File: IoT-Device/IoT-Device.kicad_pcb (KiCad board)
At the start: 4 copper layers, 100 x 70 mm, 61 parts, among them J1 USB-C, J2 Conn_01x02, J3 SWD, SW1 RESET, SW2 BOOT_MODE, SW3 B1, SW4 B2, U1 BD33GA5WEFJ, U2 STM32U585VI, U3 BQ24074RGT, U4 ESP32-C3-WROOM-02

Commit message: change two ESP32 pins for slightly more appropriate ones on STM32 (ESP_BUSY->PB2 (SPI1_RDY)
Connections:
- U2 pad 35: /ESP_RESET -> unconnected-(U2-PB0-Pad35)
- U2 pad 36: /ESP_BUSY -> /ESP_RESET
- U2 pad 37: unconnected-(U2-PB2-Pad37) -> /ESP_BUSY
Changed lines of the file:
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@@
 	(net 102 "/SWO")
 	(net 103 "/SWDIO")
-	(net 104 "unconnected-(U2-PB2-Pad37)")
-	(net 105 "/SWCLK")
-	(net 106 "unconnected-(U2-PC9-Pad66)")
-	(net 107 "unconnected-(U2-PC15-Pad9)")
-	(net 108 "Net-(D4-K)")
-	(net 109 "unconnected-(U2-PA1-Pad24)")
-	(net 110 "unconnected-(U2-PE5-Pad4)")
-	(net 111 "unconnected-(U3-ITERM-Pad15)")
-	(net 112 "unconnected-(U3-TMR-Pad14)")
-	(net 113 "Net-(U4-IO2)")
-	(net 114 "unconnected-(U4-IO18-Pad13)")
-	(net 115 "unconnected-(U4-IO1-Pad17)")
-	(net 116 "unconnected-(U4-IO19-Pad14)")
-	(net 117 "unconnected-(U4-IO0-Pad18)")
-	(net 118 "unconnected-(U4-IO3-Pad15)")
+	(net 104 "/SWCLK")
+	(net 105 "unconnected-(U2-PC9-Pad66)")
+	(net 106 "unconnected-(U2-PC15-Pad9)")
+	(net 107 "Net-(D4-K)")
+	(net 108 "unconnected-(U2-PA1-Pad24)")
+	(net 109 "unconnected-(U2-PE5-Pad4)")
+	(net 110 "unconnected-(U3-ITERM-Pad15)")
+	(net 111 "unconnected-(U3-TMR-Pad14)")
+	(net 112 "Net-(U4-IO2)")
+	(net 113 "unconnected-(U4-IO18-Pad13)")
+	(net 114 "unconnected-(U4-IO1-Pad17)")
+	(net 115 "unconnected-(U4-IO19-Pad14)")
+	(net 116 "unconnected-(U4-IO0-Pad18)")
+	(net 117 "unconnected-(U4-IO3-Pad15)")
+	(net 118 "unconnected-(U2-PB0-Pad35)")
 	(footprint "Capacitor_SMD:C_0603_1608Metric"
 		(layer "F.Cu")
@@
 			(layers "F.Cu" "F.Mask" "F.Paste")
 			(roundrect_rratio 0.25)
-			(net 110 "unconnected-(U2-PE5-Pad4)")
+			(net 109 "unconnected-(U2-PE5-Pad4)")
 			(pinfunction "PE5")
 			(pintype "bidirectional+no_connect")
@@
 			(layers "F.Cu" "F.Mask" "F.Paste")
 			(roundrect_rratio 0.25)
-			(net 107 "unconnected-(U2-PC15-Pad9)")
+			(net 106 "unconnected-(U2-PC15-Pad9)")
 			(pinfunction "PC15")
 			(pintype "bidirectional+no_connect")
@@
 			(layers "F.Cu" "F.Mask" "F.Paste")
 			(roundrect_rratio 0.25)
-			(net 109 "unconnected-(U2-PA1-Pad24)")
+			(net 108 "unconnected-(U2-PA1-Pad24)")
 			(pinfunction "PA1")
 			(pintype "bidirectional+no_connect")
@@
 			(layers "F.Cu" "F.Mask" "F.Paste")
 			(roundrect_rratio 0.25)
-			(net 36 "/ESP_RESET")
+			(net 118 "unconnected-(U2-PB0-Pad35)")
 			(pinfunction "PB0")
-			(pintype "bidirectional")
+			(pintype "bidirectional+no_connect")
 		)
 		(pad "36" smd roundrect
@@
 			(layers "F.Cu" "F.Mask" "F.Paste")
 			(roundrect_rratio 0.25)
-			(net 51 "/ESP_BUSY")
+			(net 36 "/ESP_RESET")
 			(pinfunction "PB1")
 			(pintype "bidirectional")
@@
 			(layers "F.Cu" "F.Mask" "F.Paste")
 			(roundrect_rratio 0.25)
-			(net 104 "unconnected-(U2-PB2-Pad37)")
+			(net 51 "/ESP_BUSY")
 			(pinfunction "PB2")
-			(pintype "bidirectional+no_connect")
+			(pintype "bidirectional")
 		)
 		(pad "38" smd roundrect
@@
 			(layers "F.Cu" "F.Mask" "F.Paste")
 			(roundrect_rratio 0.25)
-			(net 106 "unconnected-(U2-PC9-Pad66)")
+			(net 105 "unconnected-(U2-PC9-Pad66)")
 			(pinfunction "PC9")
 			(pintype "bidirectional+no_connect")
@@
 			(layers "F.Cu" "F.Mask" "F.Paste")
 			(roundrect_rratio 0.25)
-			(net 105 "/SWCLK")
+			(net 104 "/SWCLK")
 			(pinfunction "PA14")
 			(pintype "bidirectional")
@@
 			(size 1.5 0.9)
 			(layers "F.Cu" "F.Mask" "F.Paste")
-			(net 114 "unconnected-(U4-IO18-Pad13)")
+			(net 113 "unconnected-(U4-IO18-Pad13)")
 			(pinfunction "IO18")
 			(pintype "bidirectional+no_connect")
@@
 			(size 1.5 0.9)
 			(layers "F.Cu" "F.Mask" "F.Paste")
-			(net 116 "unconnected-(U4-IO19-Pad14)")
+			(net 115 "unconnected-(U4-IO19-Pad14)")
 			(pinfunction "IO19")
 			(pintype "bidirectional+no_connect")
@@
 			(size 1.5 0.9)
 			(layers "F.Cu" "F.Mask" "F.Paste")
-			(net 118 "unconnected-(U4-IO3-Pad15)")
+			(net 117 "unconnected-(U4-IO3-Pad15)")
 			(pinfunction "IO3")
 			(pintype "bidirectional+no_connect")
@@
 			(size 1.5 0.9)
 			(layers "F.Cu" "F.Mask" "F.Paste")
-			(net 113 "Net-(U4-IO2)")
+			(net 112 "Net-(U4-IO2)")
 			(pinfunction "IO2")
 			(pintype "bidirectional")
@@
 			(size 1.5 0.9)
 			(layers "F.Cu" "F.Mask" "F.Paste")
-			(net 115 "unconnected-(U4-IO1-Pad17)")
+			(net 114 "unconnected-(U4-IO1-Pad17)")
 			(pinfunction "IO1")
 			(pintype "bidirectional+no_connect")
@@
 			(size 1.5 0.9)
 			(layers "F.Cu" "F.Mask" "F.Paste")
-			(net 117 "unconnected-(U4-IO0-Pad18)")
+			(net 116 "unconnected-(U4-IO0-Pad18)")
 			(pinfunction "IO0")
 			(pintype "bidirectional+no_connect")
@@
 			(layers "F.Cu" "F.Mask" "F.Paste")
 			(roundrect_rratio 0.25)
-			(net 108 "Net-(D4-K)")
+			(net 107 "Net-(D4-K)")
 			(pintype "passive")
 		)
@@
 			(size 2.4 0.74)
 			(layers "F.Cu" "F.Mask" "F.Paste")
-			(net 105 "/SWCLK")
+			(net 104 "/SWCLK")
 			(pinfunction "SWCLK/TCK")
 			(pintype "output")
@@
 			(layers "F.Cu" "F.Mask" "F.Paste")
 			(roundrect_rratio 0.25)
-			(net 108 "Net-(D4-K)")
+			(net 107 "Net-(D4-K)")
 			(pinfunction "K")
 			(pintype "passive")
@@
 			(layers "F.Cu" "F.Mask" "F.Paste")
 			(roundrect_rratio 0.25)
-			(net 113 "Net-(U4-IO2)")
+			(net 112 "Net-(U4-IO2)")
 			(pintype "passive")
 		)
@@
 			(layers "F.Cu" "F.Mask" "F.Paste")
 			(roundrect_rratio 0.25)
-			(net 112 "unconnected-(U3-TMR-Pad14)")
+			(net 111 "unconnected-(U3-TMR-Pad14)")
 			(pinfunction "TMR")
 			(pintype "input+no_connect")
@@
 			(layers "F.Cu" "F.Mask" "F.Paste")
 			(roundrect_rratio 0.25)
-			(net 111 "unconnected-(U3-ITERM-Pad15)")
+			(net 110 "unconnected-(U3-ITERM-Pad15)")
 			(pinfunction "ITERM")
 			(pintype "input+no_connect")
@@
 	)
 	(segment
-		(start 39.201 84.101)
-		(end 72.1674 84.101)
+		(start 72.1674 84.101)
+		(end 39.201 84.101)
 		(width 0.2)
 		(layer "F.Cu")
@@
 	)
 	(segment
-		(start 86.825 69.4434)
-		(end 86.825 66.175)
+		(start 87.325 66.175)
+		(end 87.325 68.9434)
 		(width 0.2)
 		(layer "F.Cu")
@@
 	)
 	(segment
-		(start 72.1674 84.101)
-		(end 86.825 69.4434)
+		(start 87.325 68.9434)
+		(end 72.1674 84.101)
 		(width 0.2)
 		(layer "F.Cu")
@@
 	)
 	(segment
-		(start 38.7729 82.74)
-		(end 72.09 82.74)
+		(start 87.825 66.175)
+		(end 87.825 69.29193)
 		(width 0.2)
 		(layer "F.Cu")
@@
 	)
 	(segment
-		(start 87.325 69.79193)
-		(end 87.325 66.175)
+		(start 38.7729 82.74)
+		(end 72.09 82.74)
 		(width 0.2)
 		(layer "F.Cu")
@@
 	)
 	(segment
-		(start 36.8 80.7671)
-		(end 38.7729 82.74)
+		(start 87.825 69.29193)
+		(end 86.818465 70.298465)
 		(width 0.2)
 		(layer "F.Cu")
@@
 	)
 	(segment
-		(start 86.818465 70.298465)
-		(end 87.325 69.79193)
+		(start 36.8 80.7671)
+		(end 38.7729 82.74)
 		(width 0.2)
 		(layer "F.Cu")
@@
 		(width 0.2)
 		(layer "F.Cu")
-		(net 105)
+		(net 104)
 	)
 	(segment
@@
 		(width 0.2)
 		(layer "F.Cu")
-		(net 105)
+		(net 104)
 	)
 	(segment
@@
 		(width 0.2)
 		(layer "F.Cu")
-		(net 105)
+		(net 104)
 	)
 	(segment
@@
 		(width 0.2)
 		(layer "F.Cu")
-		(net 105)
+		(net 104)
 	)
 	(segment
@@
 		(width 0.2)
 		(layer "F.Cu")
-		(net 105)
+		(net 104)
 	)
 	(segment
@@
 		(width 0.2)
 		(layer "F.Cu")
-		(net 105)
+		(net 104)
 	)
 	(segment
@@
 		(width 0.2)
 		(layer "F.Cu")
-		(net 105)
+		(net 104)
 	)
 	(via
@@
 		(drill 0.3)
 		(layers "F.Cu" "B.Cu")
-		(net 105)
+		(net 104)
 	)
 	(via
@@
 		(drill 0.3)
 		(layers "F.Cu" "B.Cu")
-		(net 105)
+		(net 104)
 	)
 	(segment
@@
 		(width 0.2)
 		(layer "B.Cu")
-		(net 105)
+		(net 104)
 	)
 	(segment
@@
 		(width 0.2)
 		(layer "B.Cu")
-		(net 105)
+		(net 104)
 	)
 	(segment
@@
 		(width 0.2)
 		(layer "B.Cu")
-		(net 105)
+		(net 104)
 	)
 	(segment
@@
 		(width 0.2)
 		(layer "F.Cu")
-		(net 108)
+		(net 107)
 	)
 	(segment
@@
 		(width 0.2)
 		(layer "F.Cu")
-		(net 113)
+		(net 112)
 	)
 	(zone

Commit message: update SW2 GND routing
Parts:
- added R22: 10k, Resistor_SMD:R_0603_1608Metric, F.Cu at (69.9, 26.1)
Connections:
- SW2 pad 1: GND -> Net-(SW2-A)
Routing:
- net Net-(SW2-A): track 0.00 -> 2.30 mm
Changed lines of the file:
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@@
 			(drillshape 0)
 			(scaleselection 1)
-			(outputdirectory "production_manual/drill/")
+			(outputdirectory "production_manual/")
 		)
 	)
@@
 	(net 117 "unconnected-(U4-IO3-Pad15)")
 	(net 118 "unconnected-(U2-PB0-Pad35)")
+	(net 119 "Net-(SW2-A)")
 	(footprint "Capacitor_SMD:C_0603_1608Metric"
 		(layer "F.Cu")
@@
 		(descr "Ultraminiature Surface Mount Slide Switch, right-angle, https://www.ckswitches.com/media/1424/pcm.pdf")
 		(property "Reference" "SW2"
-			(at -5.9 -1.325 0)
+			(at -6.01 1.285 0)
 			(layer "F.SilkS")
 			(effects
@@
 		)
 		(property "Value" "BOOT_MODE"
-			(at -7.2 -3.225 0)
+			(at -8.76 -0.235 0)
 			(layer "F.Fab")
 			(effects
@@
 			(layer "F.Fab")
 		)
+		(fp_text user "${REFERENCE}"
+			(at 0 -3.2 180)
+			(layer "F.Fab")
+			(effects
+				(font
+					(size 1 1)
+					(thickness 0.15)
+				)
+			)
+		)
 		(pad "" smd rect
 			(at -3.65 -0.78 180)
@@
 			(size 0.7 1.5)
 			(layers "F.Cu" "F.Mask" "F.Paste")
-			(net 99 "GND")
+			(net 119 "Net-(SW2-A)")
 			(pinfunction "A")
 			(pintype "passive")
@@
 		)
 	)
+	(footprint "Resistor_SMD:R_0603_1608Metric"
+		(layer "F.Cu")
+		(at 69.88 26.1)
+		(descr "Resistor SMD 0603 (1608 Metric), square (rectangular) end terminal, IPC-7351 nominal, (Body size source: IPC-SM-782 page 72, https://www.pcb-3d.com/wordpress/wp-content/uploads/ipc-sm-782a_amendment_1_and_2.pdf), generated with kicad-footprint-generator")
+		(tags "resistor")
+		(property "Reference" "R22"
+			(at -2.87 0.64 0)
+			(layer "F.SilkS")
+			(effects
+				(font
+					(size 1 1)
+					(thickness 0.15)
+				)
+			)
+		)
+		(property "Value" "10k"
+			(at 0 1.43 0)
+			(layer "F.Fab")
+			(effects
+				(font
+					(size 1 1)
+					(thickness 0.15)
+				)
+			)
+		)
+		(property "Datasheet" "~"
+			(at 0 0 0)
+			(layer "F.Fab")
+			(hide yes)
+			(effects
+				(font
+					(size 1.27 1.27)
+					(thickness 0.15)
+				)
+			)
+		)
+		(property "Description" "Resistor"
+			(at 0 0 0)
+			(layer "F.Fab")
+			(hide yes)
+			(effects
+				(font
+					(size 1.27 1.27)
+					(thickness 0.15)
+				)
+			)
+		)
+		(property ki_fp_filters "R_*")
+		(sheetname "/")
+		(sheetfile "IoT-Device.kicad_sch")
+		(attr smd)
+		(fp_line
+			(start -0.237258 -0.5225)
+			(end 0.237258 -0.5225)
+			(stroke
+				(width 0.12)
+				(type solid)
+			)
+			(layer "F.SilkS")
+		)
+		(fp_line
+			(start -0.237258 0.5225)
+			(end 0.237258 0.5225)
+			(stroke
+				(width 0.12)
+				(type solid)
+			)
+			(layer "F.SilkS")
+		)
+		(fp_rect
+			(start -1.48 -0.73)
+			(end 1.48 0.73)
+			(stroke
+				(width 0.05)
+				(type solid)
+			)
+			(fill no)
+			(layer "F.CrtYd")
+		)
+		(fp_rect
+			(start -0.8 -0.4125)
+			(end 0.8 0.4125)
+			(stroke
+				(width 0.1)
+				(type solid)
+			)
+			(fill no)
+			(layer "F.Fab")
+		)
+		(fp_text user "${REFERENCE}"
+			(at 0 0 0)
+			(layer "F.Fab")
+			(effects
+				(font
+					(size 0.4 0.4)
+					(thickness 0.06)
+				)
+			)
+		)
+		(pad "1" smd roundrect
+			(at -0.825 0)
+			(size 0.8 0.95)
+			(layers "F.Cu" "F.Mask" "F.Paste")
+			(roundrect_rratio 0.25)
+			(net 119 "Net-(SW2-A)")
+			(pintype "passive")
+		)
+		(pad "2" smd roundrect
+			(at 0.825 0)
+			(size 0.8 0.95)
+			(layers "F.Cu" "F.Mask" "F.Paste")
+			(roundrect_rratio 0.25)
+			(net 99 "GND")
+			(pintype "passive")
+		)
+		(embedded_fonts no)
+		(model "${KICAD9_3DMODEL_DIR}/Resistor_SMD.3dshapes/R_0603_1608Metric.step"
+			(offset
+				(xyz 0 0 0)
+			)
+			(scale
+				(xyz 1 1 1)
+			)
+			(rotate
+				(xyz 0 0 0)
+			)
+		)
+	)
 	(footprint "Button_Switch_SMD:SW_SPST_PTS647_Sx50"
 		(layer "F.Cu")
@@
 	)
 	(gr_text "BOOT_MODE"
-		(at 74 25.6 0)
+		(at 75.56 22.61 0)
 		(layer "F.SilkS")
 		(effects
@@
 	)
 	(segment
+		(start 70.705 26.1)
+		(end 72.44 26.1)
+		(width 0.2)
+		(layer "F.Cu")
+		(net 99)
+	)
+	(segment
 		(start 47.05 39)
 		(end 48.02 38.03)
@@
 	)
 	(segment
-		(start 69.05 25.95)
-		(end 69 26)
-		(width 0.2)
-		(layer "F.Cu")
-		(net 99)
-	)
-	(segment
 		(start 113 73.3)
 		(end 114.9 75.2)
@@
 	)
 	(segment
+		(start 72.44 26.1)
+		(end 72.45 26.09)
+		(width 0.2)
+		(layer "F.Cu")
+		(net 99)
+	)
+	(segment
 		(start 74.85 59.3)
 		(end 73.9 59.3)
@@
 	)
 	(segment
-		(start 69.05 23.805)
-		(end 69.05 25.95)
-		(width 0.2)
-		(layer "F.Cu")
-		(net 99)
-	)
-	(segment
 		(start 83.075 38.8)
 		(end 88.325 38.8)
@@
 	)
 	(via
-		(at 69 26)
+		(at 73.8 54.9)
 		(size 0.6)
 		(drill 0.3)
@@
 	)
 	(via
-		(at 73.8 54.9)
+		(at 98 46)
 		(size 0.6)
 		(drill 0.3)
@@
 	)
 	(via
-		(at 98 46)
+		(at 60.1 21)
 		(size 0.6)
 		(drill 0.3)
@@
 	)
 	(via
-		(at 60.1 21)
+		(at 98.5 51)
 		(size 0.6)
 		(drill 0.3)
@@
 	)
 	(via
-		(at 98.5 51)
+		(at 72.45 26.09)
 		(size 0.6)
 		(drill 0.3)
@@
 		(net 112)
 	)
+	(segment
+		(start 69.055 23.81)
+		(end 69.05 23.805)
+		(width 0.2)
+		(layer "F.Cu")
+		(net 119)
+	)
+	(segment
+		(start 69.055 26.1)
+		(end 69.055 23.81)
+		(width 0.2)
+		(layer "F.Cu")
+		(net 119)
+	)
 	(zone

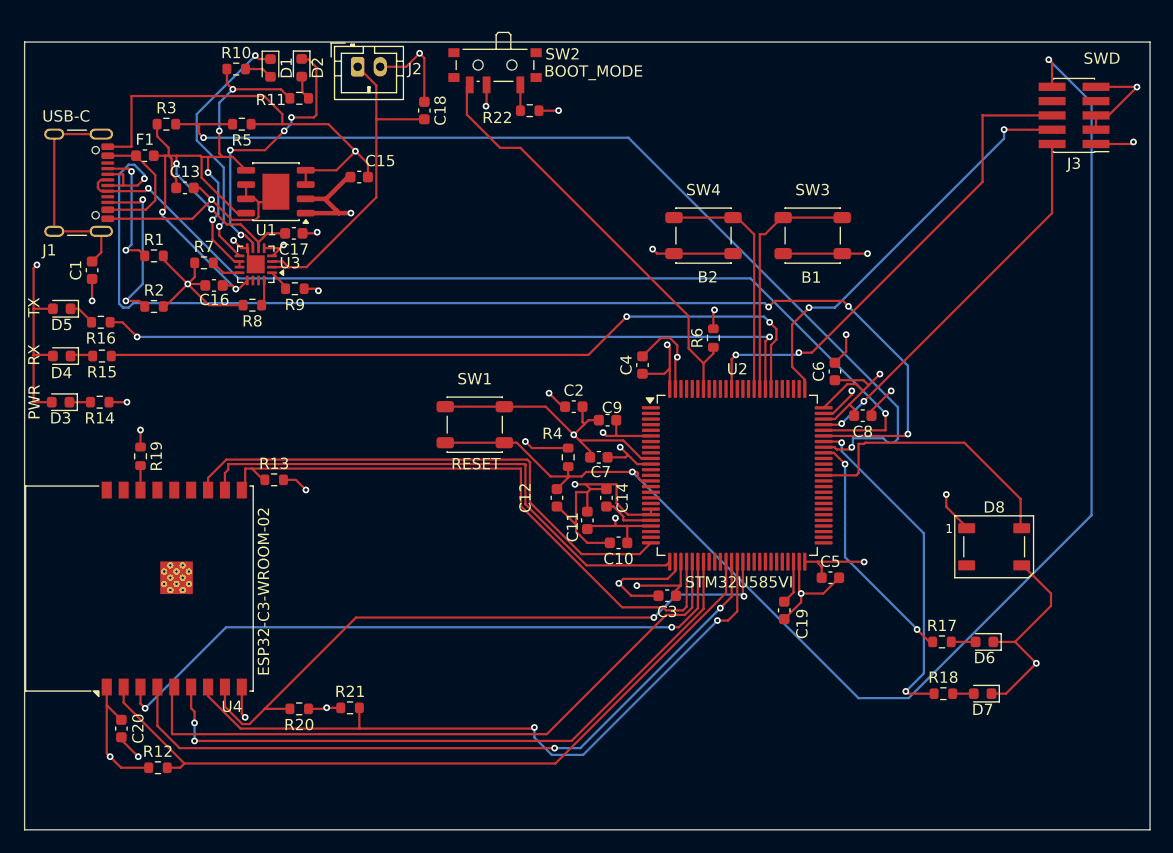
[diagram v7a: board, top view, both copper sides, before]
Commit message: connect USB-C port's CC1 and CC2 to STM32's CC1 and CC2 pins
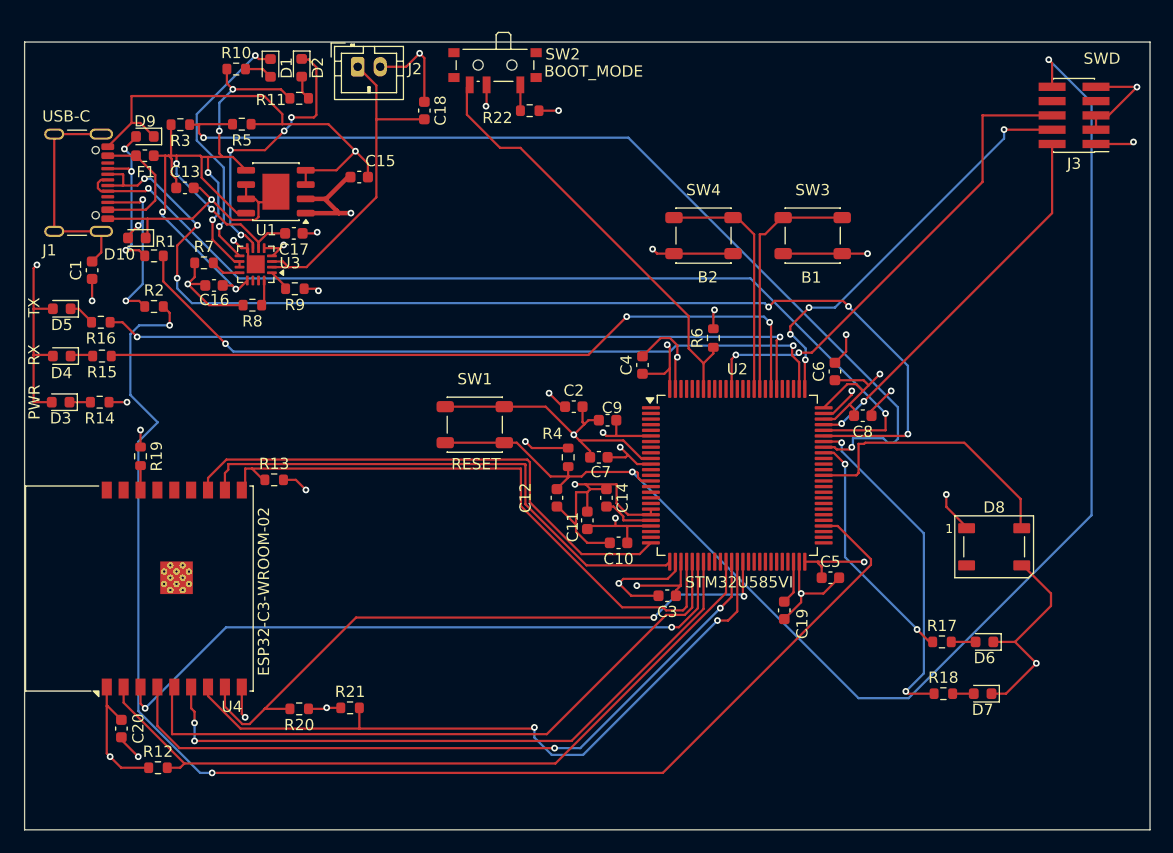
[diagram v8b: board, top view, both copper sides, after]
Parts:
- added D10: D_TVS, Diode_SMD:D_0603_1608Metric, F.Cu at (35.0, 37.4)
- added D9: D_TVS, Diode_SMD:D_0603_1608Metric, F.Cu at (35.7, 28.4)
- R1, R2: value 5.1k -> 22
- moved R3 1.24 mm to (38.8, 27.3), turned to 180 degrees
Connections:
- net /SCL renamed /I2C1_SCL
- net /SDA renamed /I2C1_SDA
- R1 pad 2: GND -> /UCPD1_CC1
- R2 pad 2: GND -> /UCPD1_CC2
- R3 pad 1: /SYS -> /MCU_VBUS
- R3 pad 2: /MCU_VBUS -> /SYS
- U2 pad 54: unconnected-(U2-PB15-Pad54) -> /UCPD1_CC2
- U2 pad 77: unconnected-(U2-PA15-Pad77) -> /UCPD1_CC1
- U2 pad 81: unconnected-(U2-PD0-Pad81) -> /TX_LED
- U2 pad 83: /TX_LED -> unconnected-(U2-PD2-Pad83)
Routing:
- net /UCPD1_CC2: track 0.00 -> 121.9 mm, vias 0 -> 2
- net /UCPD1_CC1: track 0.00 -> 65.2 mm, vias 0 -> 2
- net /OTG_DM: track 106.5 -> 99.5 mm, vias 4 -> 6
- net Net-(D9-A2): track 10.8 -> 14.6 mm, vias 2 -> 3
- net GND: track 239.6 -> 236.7 mm
- net Net-(D10-A2): track 14.2 -> 16.3 mm, vias 2 -> 3
- net /MCU_VBUS: track 88.7 -> 87.5 mm
- net /TX_LED: track 63.9 -> 64.7 mm
- net /SWCLK: track 36.9 -> 37.2 mm, vias 2 -> 4
